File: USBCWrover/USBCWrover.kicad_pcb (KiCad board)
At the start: 2 copper layers, 21 parts, among them J1 USB_C_Receptacle_USB2.0, Q1 Q_NMOS_GSD, Q2 Q_NMOS_GSD, SW1 SW_Push, SW2 SW_Push, U1 CH340C, U2 CP2104, U3 AMS1117-3.3

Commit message: routing done, but not pretty
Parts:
- removed C3: 100nF, Capacitor_SMD:C_0603_1608Metric
- removed Q1, Q2: Q_NMOS_GSD, Package_TO_SOT_SMD:SOT-23
- removed R3, R4: 10k, Resistor_SMD:R_0603_1608Metric
- removed SW2: SW_Push, Button_Switch_SMD:SW_Push_1P1T_NO_6x6mm_H9.5mm
- added J2: Conn_02x10_Odd_Even, Connector_PinHeader_2.54mm:PinHeader_2x10_P2.54mm_Vertical, B.Cu at (154.9, 106.7)
- added J3: Conn_02x10_Odd_Even, Connector_PinHeader_2.54mm:PinHeader_2x10_P2.54mm_Vertical, B.Cu at (129.5, 106.7)
- added U4: ESP32-WROVER, esp32-wrover:ESP32-WROVER, F.Cu at (141.0, 105.1)
- U1: value CH340C -> UMH3N; footprint Package_SO:SOIC-16_3.9x9.9mm_P1.27mm -> Package_SO:TSOP-6_1.65x3.05mm_P0.95mm
- moved J1 39.2 mm to (141.9, 144.3)
- moved U3 36.5 mm to (151.9, 142.2), turned to 270 degrees
- moved R6 35.5 mm to (128.1, 135.8)
- moved U2 32.3 mm to (141.7, 134.5), turned to 90 degrees
- moved R5 29.5 mm to (128.1, 133.3)
- moved U1 27.4 mm to (132.6, 134.6)
- moved SW1 26.2 mm to (130.9, 142.3)
- moved C4 21.9 mm to (150.1, 135.9)
- moved C1 20.9 mm to (146.5, 133.3)
- moved C7 19.9 mm to (154.2, 135.9)
- moved C2 17.8 mm to (136.9, 133.3), turned to 180 degrees
- moved R2 17.2 mm to (146.5, 135.9), turned to 180 degrees
- moved R1 17.1 mm to (136.9, 135.8)
- moved C5 15.5 mm to (150.1, 133.4)
- moved C6 14.9 mm to (154.2, 133.4)
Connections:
- U1 pad 1: GND -> SER_RTS
- U1 pad 2: ESP_RXD -> SER_DTR
- U1 pad 3: ESP_TXD -> ESP_FLS
- U1 pad 4: Net-(U1-Pad4) -> SER_DTR
- U1 pad 5: USB_D+ -> SER_RTS
- U1 pad 6: USB_D- -> ESP_RST
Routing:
- net +3V3: track 0.00 -> 90.0 mm, vias 0 -> 4
- net ESP_RST: track 0.00 -> 53.7 mm, vias 0 -> 4
- net +5V: track 0.00 -> 41.4 mm, vias 0 -> 4
- net ESP_RXD: track 0.00 -> 40.1 mm, vias 0 -> 2
- net ESP_TXD: track 0.00 -> 35.0 mm, vias 0 -> 4
- net ESP_FLS: track 0.00 -> 34.9 mm, vias 0 -> 2
- net IO18: track 0.00 -> 29.6 mm, vias 0 -> 3
- net IO27: track 0.00 -> 28.0 mm, vias 0 -> 1
- net IO19: track 0.00 -> 27.6 mm, vias 0 -> 1
- net IO23: track 0.00 -> 27.6 mm, vias 0 -> 1
- net IO25: track 0.00 -> 25.5 mm, vias 0 -> 3
- net IO12: track 0.00 -> 25.3 mm, vias 0 -> 1
- net IO32: track 0.00 -> 25.3 mm, vias 0 -> 1
- net IO5: track 0.00 -> 23.0 mm, vias 0 -> 3
- net GND: track 0.00 -> 20.1 mm, vias 0 -> 23
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- added copper zone on B.Cu, net GND
- added copper zone on F.Cu, net GND
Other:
- board outline added: 31.5 x 42 mm
- net class Default: clearance 0.2 -> 0.127
- rule trace_clearance: 0.2 -> 0.127

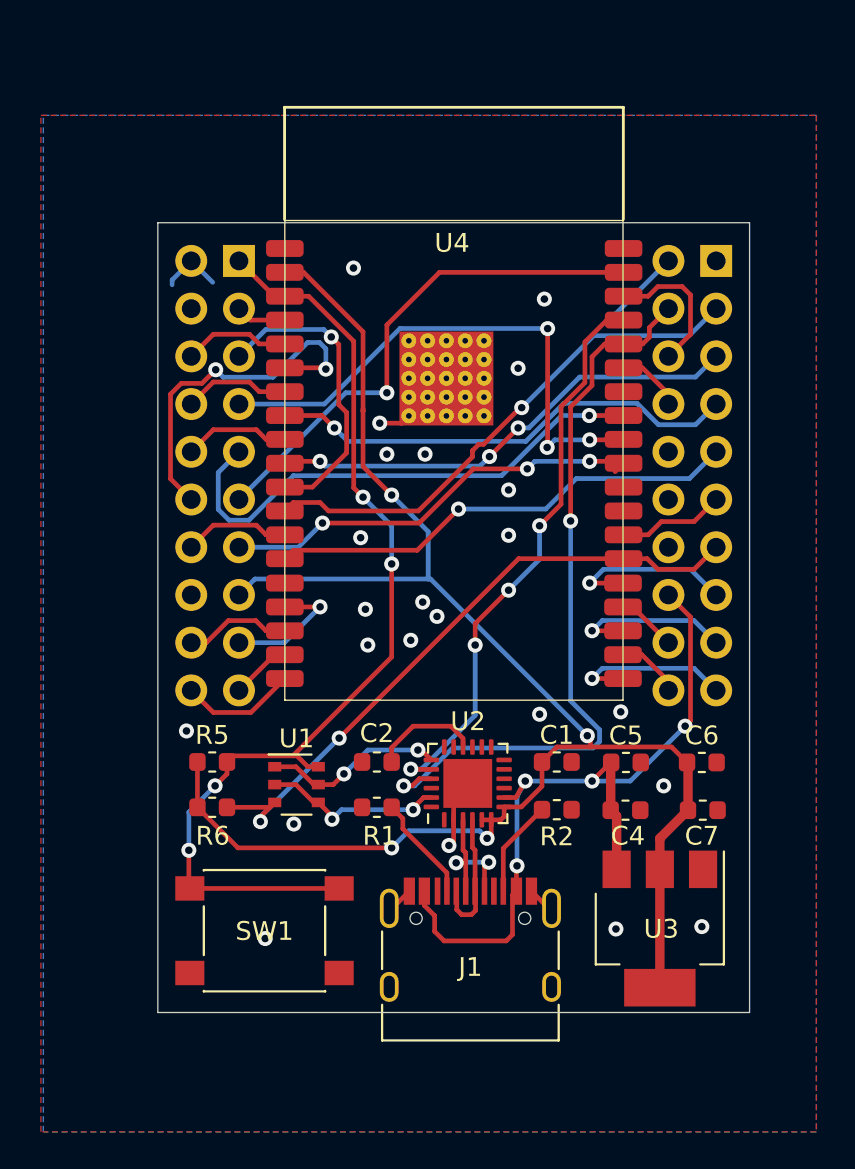
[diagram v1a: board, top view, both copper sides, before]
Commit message: added silkscreen back
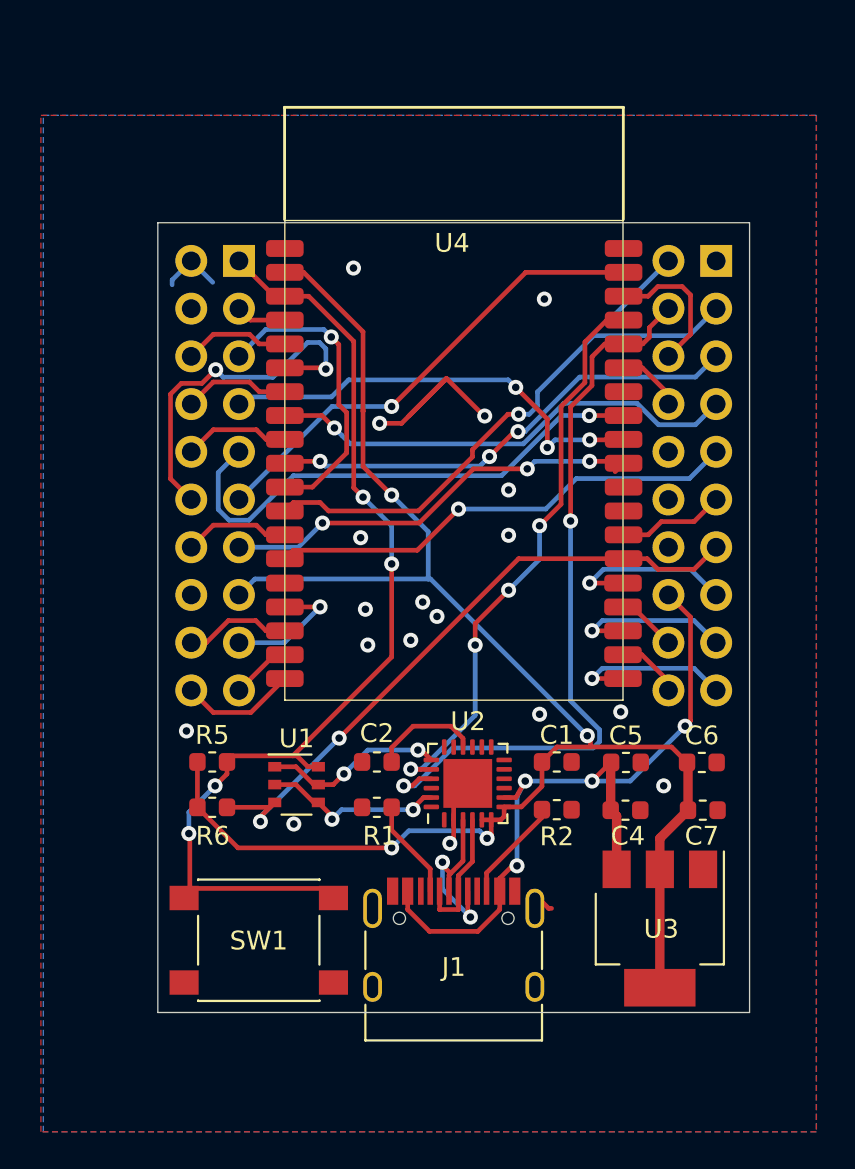
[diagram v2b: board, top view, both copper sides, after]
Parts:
- moved J1 0.89 mm to (141.0, 144.3)
- moved SW1 0.59 mm to (130.6, 142.8)
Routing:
- net IO18: track 29.6 -> 24.5 mm
- net IO23: track 27.6 -> 25.5 mm
- net USB_D+: track 7.76 -> 9.85 mm
- net GND: track 20.1 -> 18.5 mm, vias 23 -> 18
- net +5V: track 41.4 -> 40.6 mm
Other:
- board text added: "GND IO27 IO25 IO32 TDI IO4 IO0 IO2 SD1 CLK"
- board text added: "GND NC SVN IO35 IO33 IO34 TMS NC SD2 CMD"
- board text added: "RST SVP IO26 IO18 IO19 IO23 IO5 3.3v TCK SD3"
- board text added: "TXD RXD IO22 IO21 NC NC GND 5V TDD SD0"
- board text added: "https://git.io/JJAKG"

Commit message: lot prettier
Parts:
- added G***: LOGO, parts_models:wemos_balkje, B.Cu at (129.5, 115.6)
- added G***: LOGO, parts_models:wemos_balkje, B.Cu at (152.4, 115.6)
- added G***: LOGO, parts_models:wemos_balkje, F.Cu at (129.5, 115.6)
- added G***: LOGO, parts_models:wemos_balkje, F.Cu at (152.4, 115.6)
- U3: value AMS1117-3.3 -> HX9193-33GB; footprint Package_TO_SOT_SMD:SOT-223-3_TabPin2 -> Package_TO_SOT_SMD:SOT-23-5
- moved U3 8.42 mm to (150.9, 133.9), turned to 180 degrees
- moved C6 8.36 mm to (145.9, 132.1), turned to 90 degrees
- moved C7 7.46 mm to (147.8, 132.1), turned to 90 degrees
- moved C4 4.66 mm to (154.7, 135.0)
- moved C5 4.55 mm to (154.7, 132.8)
- moved R5 4.10 mm to (132.2, 133.6), turned to 90 degrees
- moved U1 3.42 mm to (129.3, 133.7)
- moved R6 2.78 mm to (126.4, 133.6), turned to 90 degrees
- moved C1 2.75 mm to (144.0, 132.1), turned to 90 degrees
- moved C2 2.15 mm to (134.9, 132.6)
- moved R1 2.12 mm to (134.9, 135.1)
- moved SW1 2.00 mm to (130.6, 140.8)
- moved R2 1.84 mm to (144.8, 135.1)
- moved J1 1.78 mm to (141.1, 142.5)
- moved U2 1.50 mm to (140.3, 133.9)
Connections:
- J2 pad 10: Net-(J2-Pad10) -> IO17
- J2 pad 12: Net-(J2-Pad12) -> IO16
- U3 pad 1: GND -> +5V
- U3 pad 2: +3V3 -> GND
- U4 pad 27: Net-(U4-Pad27) -> IO16
- U4 pad 28: Net-(U4-Pad28) -> IO17
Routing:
- net GND: track 18.5 -> 64.3 mm, vias 18 -> 15
- net +3V3: track 90.0 -> 78.1 mm, vias 4 -> 5
- net SER_RTS: track 9.71 -> 16.9 mm
- net USB_D+: track 9.85 -> 6.02 mm
- net IO17: track 0.00 -> 3.17 mm
- net ESP_RST: track 53.7 -> 50.8 mm
- net Net-(J1-PadA5): track 5.31 -> 8.10 mm, vias 0 -> 2
- net IO16: track 0.00 -> 2.64 mm
- net USB_D-: track 7.06 -> 9.30 mm
- net ESP_TXD: track 35.0 -> 37.2 mm
- net SER_DTR: track 9.73 -> 11.8 mm
- net ESP_FLS: track 34.9 -> 36.7 mm
- net Net-(J1-PadB5): track 5.56 -> 3.80 mm
- net ESP_RXD: track 40.1 -> 38.3 mm
- net +5V: track 40.6 -> 41.3 mm, vias 4 -> 0
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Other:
- board size 31.5 x 42 mm -> 31.5 x 40.5 mm
- board text added: "JLCJLCJLCJLC"
- board text added: "Reset"
- board text added: "TXD RXD IO22 IO21 IO17* IO16* GND 5V TDD SD0"
- board text added: "Wroom / Wrover"
- board text removed: "TXD RXD IO22 IO21 NC NC GND 5V TDD SD0"

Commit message: now with art
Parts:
- removed the G*** at (129.5, 115.6) (x2)
- removed the G*** at (152.4, 115.6) (x2)
- added D1: SK6812, LED_SMD:LED_SK6812_PLCC4_5.0x5.0mm_P3.2mm, F.Cu at (150.7, 139.3)
- added G***: LOGO, parts_models:SnekMugHug_FIX_F.Cu_F.Mask, F.Cu at (151.3, 140.3)
- added TP1: TestPoint, TestPoint:TestPoint_Pad_2.0x2.0mm, B.Cu at (141.5, 142.9)
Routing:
- net IO15: track 3.20 -> 17.8 mm
- net Net-(D1-Pad4): track 0.00 -> 7.63 mm
- net +5V: track 41.3 -> 43.7 mm, vias 0 -> 1
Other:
- board text added: "LEDdata"

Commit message: rework
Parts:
- removed C1: 100nF, Capacitor_SMD:C_0603_1608Metric
- removed C2: 4.7uF, Capacitor_SMD:C_0603_1608Metric
- removed R1, R2: 5.1k, Resistor_SMD:R_0603_1608Metric
- removed R5, R6: 10k, Resistor_SMD:R_0603_1608Metric
- removed SW1: SW_Push, Button_Switch_SMD:SW_Push_1P1T_NO_6x6mm_H9.5mm
- added D2: b5819w, Diode_SMD:D_SOD-123, F.Cu at (145.3, 135.5)
- added RN1: R_Pack04, Resistor_SMD:R_Array_Concave_4x0603, F.Cu at (128.3, 135.6)
- added SW2: SW_Push, Button_Switch_SMD:SW_Push_1P1T_NO_CK_KSC6xxJ, F.Cu at (130.4, 141.9)
- C4, C5, C6, C7: footprint Capacitor_SMD:C_0603_1608Metric -> Capacitor_SMD:C_0805_2012Metric
- J2, J3: footprint Connector_PinHeader_2.54mm:PinHeader_2x10_P2.54mm_Vertical -> Connector_PinHeader_2.54mm:PinHeader_2x09_P2.54mm_Vertical
- TP1: footprint TestPoint:TestPoint_Pad_2.0x2.0mm -> TestPoint:TestPoint_Pad_1.0x1.0mm
- U2: value CP2104 -> CH340C; footprint Package_DFN_QFN:QFN-24-1EP_4x4mm_P0.5mm_EP2.6x2.6mm -> Package_SO:SOIC-16_3.9x9.9mm_P1.27mm
- moved TP1 8.46 mm to (149.7, 145.0)
- moved C4 4.53 mm to (153.5, 130.6)
- moved U2 4.17 mm to (136.2, 133.5)
- moved U3 2.74 mm to (149.5, 131.5)
- moved U1 2.62 mm to (128.2, 131.3), turned to 180 degrees
- moved C6 2.18 mm to (143.9, 131.4)
- moved C7 1.87 mm to (146.1, 131.4)
- moved D1 1.84 mm to (151.7, 140.9)
- moved J2 1.32 mm to (154.9, 105.4)
- moved J3 1.32 mm to (129.5, 105.4)
- moved U4 1.32 mm to (141.0, 103.8)
- moved C5 1.23 mm to (153.5, 132.5)
- moved G*** 1.22 mm to (151.7, 141.5)
- moved J1 0.36 mm to (141.1, 142.8)
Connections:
- J1 pad A4: +5V -> VUSB
- J1 pad A5: Net-(J1-PadA5) -> CC1
- J1 pad A8: Net-(J1-PadA8) -> (no net)
- J1 pad A9: +5V -> VUSB
- J1 pad B4: +5V -> VUSB
- J1 pad B5: Net-(J1-PadB5) -> CC2
- J1 pad B8: Net-(J1-PadB8) -> (no net)
- J1 pad B9: +5V -> VUSB
- J2 pad 10: IO17 -> (no net)
- J2 pad 12: IO16 -> (no net)
- J2 pad 17: SD1_IO8 -> (no net)
- J3 pad 16: Net-(J3-Pad16) -> (no net)
- J3 pad 18: SD2_IO9 -> (no net)
- J3 pad 4: Net-(J3-Pad4) -> (no net)
- U2 pad 1: Net-(U2-Pad1) -> GND
- U2 pad 10: Net-(U2-Pad10) -> (no net)
- U2 pad 11: Net-(U2-Pad11) -> (no net)
- U2 pad 12: Net-(U2-Pad12) -> (no net)
- U2 pad 13: Net-(U2-Pad13) -> SER_DTR
- U2 pad 14: Net-(U2-Pad14) -> SER_RTS
- U2 pad 15: Net-(U2-Pad15) -> (no net)
- U2 pad 16: Net-(C2-Pad1) -> +3V3
- U2 pad 2: GND -> ESP_RXD
- U2 pad 3: USB_D+ -> ESP_TXD
- U2 pad 4: USB_D- -> +3V3
- U2 pad 5: +3V3 -> USB_D+
- U2 pad 6: +3V3 -> USB_D-
- U2 pad 7: +3V3 -> (no net)
- U2 pad 8: +5V -> (no net)
- U2 pad 9: Net-(U2-Pad9) -> (no net)
- U3 pad 4: Net-(U3-Pad4) -> (no net)
- U4 pad 17: SD2_IO9 -> (no net)
- U4 pad 18: SD3_IO10 -> (no net)
- U4 pad 19: CMD_IO11 -> (no net)
- U4 pad 20: CLK_IO6 -> (no net)
- U4 pad 21: SD0_IO7 -> (no net)
- U4 pad 22: SD1_IO8 -> (no net)
- U4 pad 27: IO16 -> (no net)
- U4 pad 28: IO17 -> (no net)
- U4 pad 32: Net-(U4-Pad32) -> (no net)
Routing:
- net GND: track 64.3 -> 0.00 mm
- net CC2: track 0.00 -> 18.8 mm
- net CC1: track 0.00 -> 15.6 mm
- net +5V: track 43.7 -> 30.4 mm
- net VUSB: track 0.00 -> 10.9 mm, vias 0 -> 2
- net SD1_IO8: track 8.96 -> 0.00 mm, vias 1 -> 0
- net CLK_IO6: track 8.96 -> 0.00 mm, vias 1 -> 0
- net Net-(J1-PadA5): track 8.10 -> 0.00 mm, vias 2 -> 0
- net SER_RTS: track 16.9 -> 9.47 mm, vias 2 -> 0
- net IO34: track 19.2 -> 12.7 mm, vias 2 -> 0
- net Net-(C2-Pad1): track 6.35 -> 0.00 mm
- net CMD_IO11: track 6.22 -> 0.00 mm
- net SD2_IO9: track 5.69 -> 0.00 mm
- net Net-(D1-Pad4): track 7.63 -> 2.92 mm
- net USB_D+: track 6.02 -> 10.7 mm, vias 2 -> 0
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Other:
- board size 31.5 x 40.5 mm -> 31.9 x 49.9 mm
- board text added: "GND IO27 IO25 IO32 IO12 IO4 IO0 IO2 NC"
- board text added: "GND NC I 39 I 35 IO33 I 34 IO14 NC NC"
- board text added: "RST I 36 IO26 IO18 IO19 IO23 IO5 3.3v IO13"
- board text added: "TXD RXD IO22 IO21 NC NC GND 5V IO15"
- board text added: "Wrover"
- board text removed: "GND IO27 IO25 IO32 TDI IO4 IO0 IO2 SD1 CLK"
- board text removed: "GND NC SVN IO35 IO33 IO34 TMS NC SD2 CMD"
- board text removed: "RST SVP IO26 IO18 IO19 IO23 IO5 3.3v TCK SD3"
- board text removed: "TXD RXD IO22 IO21 IO17* IO16* GND 5V TDD SD0"
- board text removed: "Wroom / Wrover"

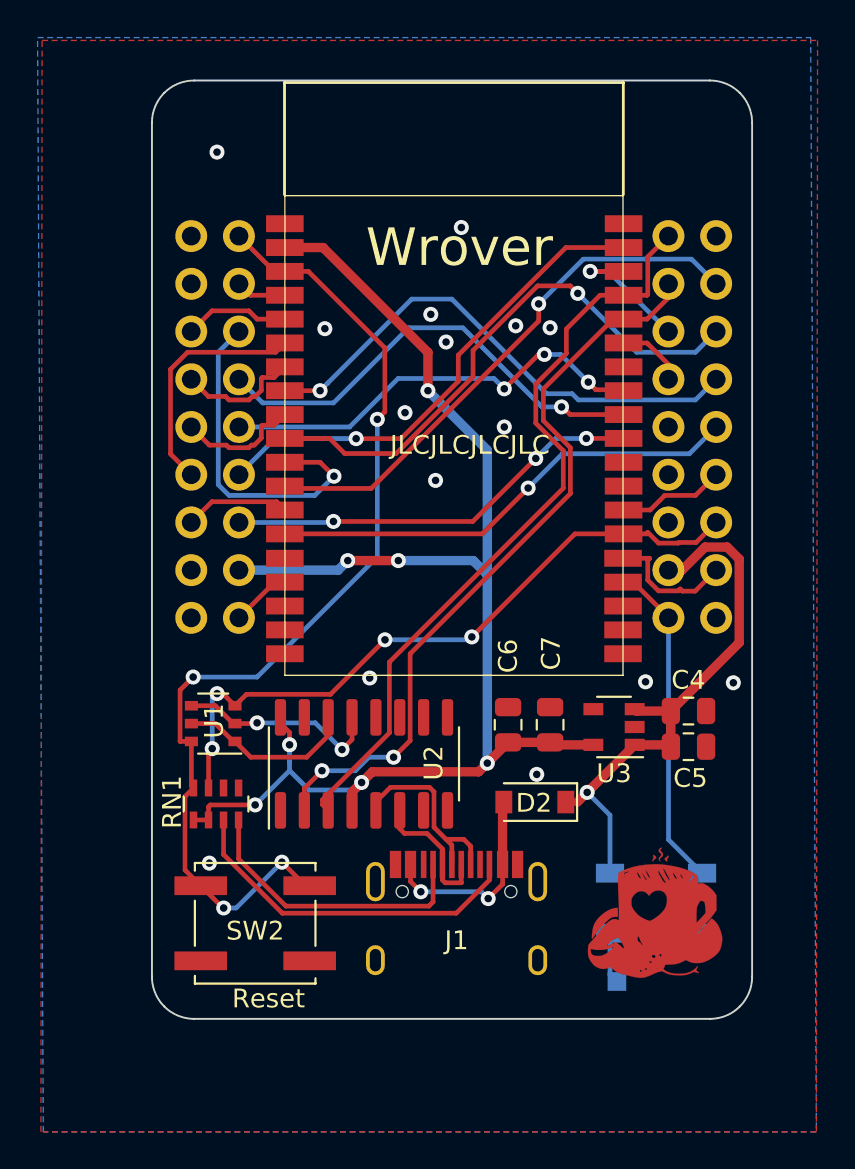
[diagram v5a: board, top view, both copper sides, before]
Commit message: pads with text on top, resistor network instead of 4 resistors, usb serial rerouted
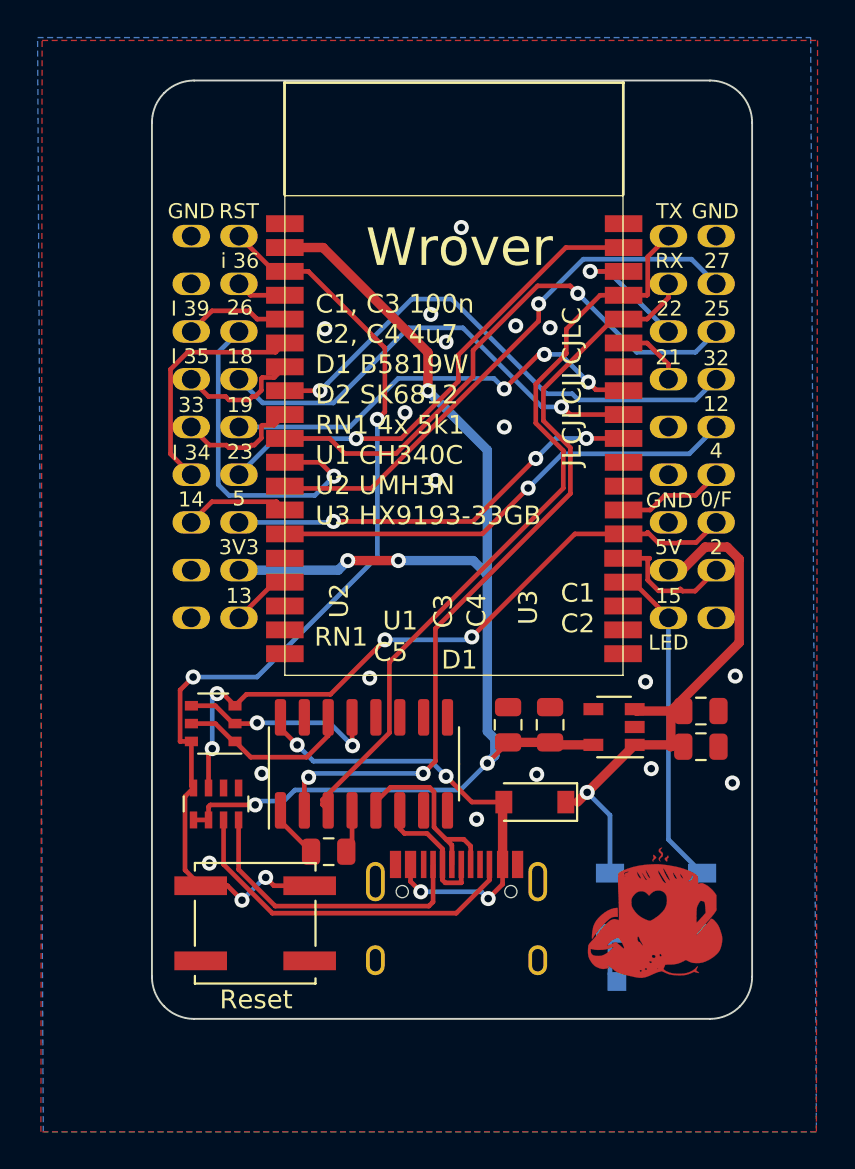
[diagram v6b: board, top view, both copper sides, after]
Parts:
- added C5: 100nF, Capacitor_SMD:C_0805_2012Metric, F.Cu at (134.3, 138.1)
- moved C1 0.66 mm to (154.1, 130.6)
- moved C2 0.66 mm to (154.1, 132.5)
- renumbered C4 to C1, C5 to C2, C6 to C3, C7 to C4, D2 to D1, D1 to D2, SW2 to SW1, U2 to U1, U1 to U2
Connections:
- J1 pad A8: (no net) -> Net-(J1-PadA8)
- J1 pad B8: (no net) -> Net-(J1-PadB8)
- J2 pad 10: (no net) -> Net-(J2-Pad10)
- J2 pad 12: (no net) -> Net-(J2-Pad12)
- J2 pad 17: (no net) -> Net-(J2-Pad17)
- J3 pad 16: (no net) -> Net-(J3-Pad16)
- J3 pad 18: (no net) -> Net-(J3-Pad18)
- J3 pad 4: (no net) -> Net-(J3-Pad4)
- U1 pad 10: (no net) -> Net-(U1-Pad10)
- U1 pad 11: (no net) -> Net-(U1-Pad11)
- U1 pad 12: (no net) -> Net-(U1-Pad12)
- U1 pad 15: (no net) -> Net-(U1-Pad15)
- U1 pad 16: +3V3 -> VUSB
- U1 pad 4: +3V3 -> Net-(C5-Pad2)
- U1 pad 7: (no net) -> Net-(U1-Pad7)
- U1 pad 8: (no net) -> Net-(U1-Pad8)
- U1 pad 9: (no net) -> Net-(U1-Pad9)
- U3 pad 4: (no net) -> Net-(U3-Pad4)
- U4 pad 17: (no net) -> Net-(U4-Pad17)
- U4 pad 18: (no net) -> Net-(U4-Pad18)
- U4 pad 19: (no net) -> Net-(U4-Pad19)
- U4 pad 20: (no net) -> Net-(U4-Pad20)
- U4 pad 21: (no net) -> Net-(U4-Pad21)
- U4 pad 22: (no net) -> Net-(U4-Pad22)
- U4 pad 27: (no net) -> Net-(U4-Pad27)
- U4 pad 28: (no net) -> Net-(U4-Pad28)
- U4 pad 32: (no net) -> Net-(U4-Pad32)
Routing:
- net VUSB: track 10.9 -> 25.0 mm, vias 2 -> 4
- net +3V3: track 75.9 -> 70.6 mm, vias 7 -> 5
- net GND: track 0.00 -> 2.87 mm, vias 15 -> 18
- net Net-(C5-Pad2): track 0.00 -> 2.40 mm
- net ESP_RXD: track 40.1 -> 41.8 mm
- net ESP_RST: track 54.4 -> 53.3 mm
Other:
- board text added: "0/F"
- board text added: "12"
- board text added: "13"
- board text added: "14"
- board text added: "15"
- board text added: "18"
- board text added: "19"
- board text added: "2"
- board text added: "21"
- board text added: "22"
- board text added: "23"
- board text added: "25"
- board text added: "26"
- board text added: "27"
- board text added: "32"
- board text added: "33"
- board text added: "3V3"
- board text added: "4"
- board text added: "5"
- board text added: "5V"
- board text added: "C1, C3 100n C2, C4 4u7 D1 B5819W D2 SK6812 RN1 4x 5k1 U1 CH340C U2 UMH3N U3 HX9193-33GB"
- board text added: "GND"
- board text added: "I 34"
- board text added: "I 35"
- board text added: "I 39"
- board text added: "LED"
- board text added: "LedOut"
- board text added: "RST"
- board text added: "RX"
- board text added: "TX"
- board text added: "i 36"
- board text added: "reverse!"
- board text removed: "LEDdata"

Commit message: redesign
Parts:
- removed TP1: TestPoint, TestPoint:TestPoint_Pad_1.0x1.0mm
- added D3: LED, LED_SMD:LED_1206_3216Metric_ReverseMount_Hole1.8x2.4mm, B.Cu at (151.4, 140.8)
- added G***: LOGO, parts_models:revspace_led_5mm, B.Cu at (133.1, 143.0)
- added G***: LOGO, parts_models:revspace_name_5mm, B.Cu at (129.8, 144.3)
- added G***: LOGO, parts_models:revspace_name_5mm, F.Cu at (153.4, 100.6)
- added G***: LOGO, parts_models:revspace_led_5mm, F.Cu at (128.5, 100.6)
- added R1: R, Resistor_SMD:R_0805_2012Metric_Pad1.15x1.40mm_HandSolder, B.Cu at (147.3, 143.5)
- moved SW1 1.32 mm to (130.4, 143.3)
- moved C5 0.55 mm to (133.9, 138.4)
- moved C2 0.30 mm to (154.1, 132.8)
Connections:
- J2 pad 17: Net-(J2-Pad17) -> Net-(D2-Pad4)
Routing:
- net Net-(D2-Pad4): track 2.92 -> 26.6 mm
- net ESP_TXD: track 41.0 -> 49.4 mm, vias 0 -> 1
- net ESP_RST: track 53.3 -> 57.1 mm
- net IO2: track 7.05 -> 10.2 mm, vias 0 -> 1
- net Net-(D3-Pad1): track 0.00 -> 3.15 mm
- net IO15: track 17.6 -> 20.5 mm
- net GND: track 2.87 -> 0.00 mm
- net IO25: track 29.7 -> 32.0 mm
- net +5V: track 30.4 -> 32.1 mm
- net CC2: track 19.2 -> 20.5 mm
- net CC1: track 15.9 -> 17.1 mm
- net IO33: track 6.54 -> 5.41 mm
- net IO35: track 6.54 -> 5.41 mm
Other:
- board text added: "A"
- board text added: "I 36"
- board text added: "K"
- board text added: "OUT"
- board text added: "R"
- board text removed: "LedOut"
- board text removed: "i 36"
